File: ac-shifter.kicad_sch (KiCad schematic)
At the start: 12 parts, among them U13 LM393

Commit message: schem/pcb: update MB10S footprint
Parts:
- D8: footprint Pers:SOIC245P670X290-4N -> Package_SO:OnSemi_751EP_SOIC-4_3.9x4.725mm_P2.54mm
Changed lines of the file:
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@@
 			)
 		)
-		(property "Footprint" "Pers:SOIC245P670X290-4N"
+		(property "Footprint" "Package_SO:OnSemi_751EP_SOIC-4_3.9x4.725mm_P2.54mm"
 			(at 92.71 93.98 0)
 			(effects

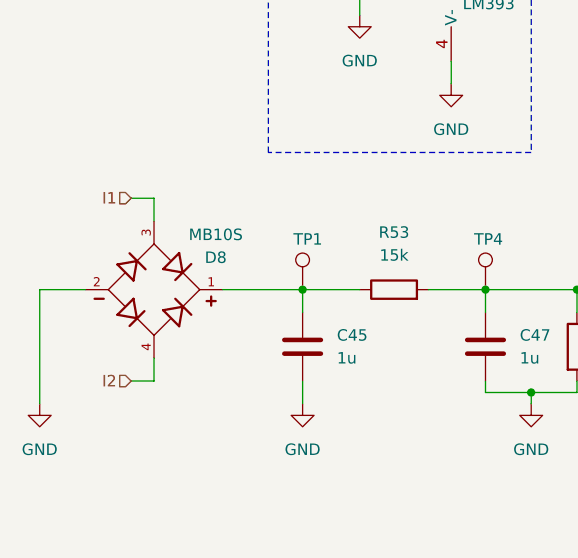
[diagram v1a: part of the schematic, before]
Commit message: pcb: ac level shifter layout
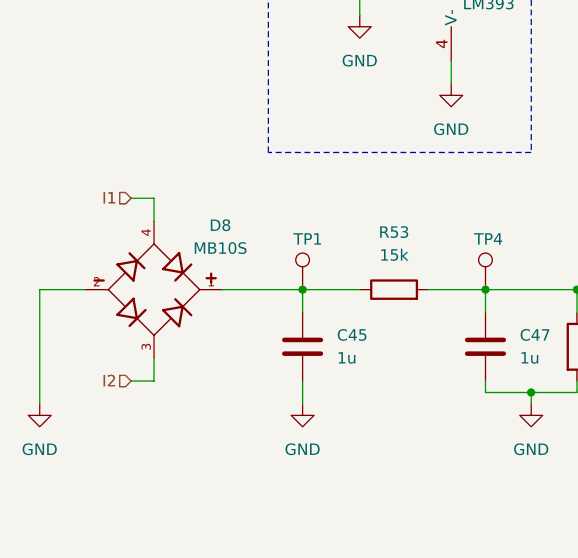
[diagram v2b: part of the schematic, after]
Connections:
- net I1: now also D8.4; no longer D8.3
- net I2: now also D8.3; no longer D8.4
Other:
- moved on the sheet: D8
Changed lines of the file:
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@@
 	(symbol
 		(lib_id "Pers:MB10S")
-		(at 92.71 93.98 180)
+		(at 92.71 93.98 0)
+		(mirror y)
 		(unit 1)
 		(exclude_from_sim no)
@@
 		(dnp no)
 		(property "Reference" "D8"
-			(at 99.568 90.424 0)
+			(at 100.076 86.868 0)
 			(effects
 				(font
@@
 		)
 		(property "Value" "MB10S"
-			(at 99.568 87.884 0)
+			(at 100.076 89.408 0)
 			(effects
 				(font
